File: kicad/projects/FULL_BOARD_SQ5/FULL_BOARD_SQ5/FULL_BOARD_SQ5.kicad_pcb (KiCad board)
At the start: 2 copper layers, 190 parts, among them J2 UART, J4 CONN_2x1, Q1 BC847, SW1 TL3342F450QG, U1 24LC512, U10 HALL_SENSOR_6, U11 HALL_SENSOR_10, U12 HALL_SENSOR_14, U13 HALL_SENSOR3, U14 HALL_SENSOR7, U15 HALL_SENSOR11, U16 HALL_SENSOR15, U17 HALL_SENSOR4, U18 HALL_SENSOR8, U19 HALL_SENSOR12, U2 STM32L431CCTx, U20 HALL_SENSOR16, U21 CD74HC4067M, U22 HALL_SENSOR_1, U23 HALL_SENSOR_5, U24 HALL_SENSOR_9, U25 HALL_SENSOR_13, U26 HALL_SENSOR_2, U27 HALL_SENSOR_6, U28 HALL_SENSOR_10, U29 HALL_SENSOR_14, U3 AP2112K-3.3, U30 HALL_SENSOR3, U31 HALL_SENSOR7, U32 HALL_SENSOR11, U33 HALL_SENSOR15, U34 HALL_SENSOR4, U35 HALL_SENSOR8, U36 HALL_SENSOR12, U37 HALL_SENSOR16, U38 CD74HC4067M, U39 HALL_SENSOR_1, U4 AP2112K-3.3, U40 HALL_SENSOR_5, U41 HALL_SENSOR_9, U42 HALL_SENSOR_13, U43 HALL_SENSOR_2, U44 HALL_SENSOR_6, U45 HALL_SENSOR_10, U46 HALL_SENSOR_14, U47 HALL_SENSOR3, U48 HALL_SENSOR7, U49 HALL_SENSOR11, U5 HALL_SENSOR_1, U50 HALL_SENSOR15, U51 HALL_SENSOR4, U52 HALL_SENSOR8, U53 HALL_SENSOR12, U54 HALL_SENSOR16, U55 CD74HC4067M, U56 HALL_SENSOR_1, U57 HALL_SENSOR_5, U58 HALL_SENSOR_9, U59 HALL_SENSOR_13, U6 HALL_SENSOR_5, U60 HALL_SENSOR_2, U61 HALL_SENSOR_6, U62 HALL_SENSOR_10, U63 HALL_SENSOR_14, U64 HALL_SENSOR3, U65 HALL_SENSOR7, U66 HALL_SENSOR11, U67 HALL_SENSOR15, U68 HALL_SENSOR4, U69 HALL_SENSOR8, U7 HALL_SENSOR_9, U70 HALL_SENSOR12, U71 HALL_SENSOR16, U72 CD74HC4067M, U8 HALL_SENSOR_13, U9 HALL_SENSOR_2

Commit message: saving work
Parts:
- removed U2: STM32L431CCTx, Package_QFP:LQFP-48_7x7mm_P0.5mm
- added D2: PESD5V0L2BT, PCM_Package_TO_SOT_SMD_AKL:SOT-23, F.Cu at (234.8, 163.9)
- added D7: TVS3V3L4U, PCM_Package_SO_AKL:TSOP-6_1.65x3.05mm_P0.95mm, F.Cu at (234.8, 159.1)
- added J1: Conn_ARM_JTAG_SWD_10, BD125-10-A-0305-0580-L-B:GCT_BD125-10-A-0305-0580-L-B, F.Cu at (233.1, 178.0)
- added J3: USB_C_Receptacle_USB2.0_16P, Connector_USB:USB_C_Receptacle_GCT_USB4105-xx-A_16P_TopMnt_Horizontal, F.Cu at (218.5, 162.1)
- added LS1: CMT-1203-SMT, CMT-1203-SMT:CUI_CMT-1203-SMT, F.Cu at (219.5, 148.5)
- added U73: STM32L433CCTx, Package_QFP:LQFP-48_7x7mm_P0.5mm, F.Cu at (218.4, 172.4)
- added Y1: NX3215SA-32.768KHZ-EXS00A-MU00525, PCM_Crystal_AKL:Crystal_SMD_MicroCrystal_CC7V-T1A-2Pin_3.2x1.5mm_HandSoldering, F.Cu at (234.4, 154.2)
- moved U51 102.5 mm to (303.7, 143.5)
- moved U52 102.5 mm to (303.7, 149.3)
- moved U53 102.5 mm to (303.7, 155.1)
- moved U54 102.5 mm to (303.7, 160.8)
- moved U55 102.5 mm to (288.7, 172.0)
- moved R18 102.5 mm to (297.5, 164.9)
- moved U39 102.5 mm to (284.2, 143.5)
- moved U40 102.5 mm to (284.2, 149.3)
- moved U41 102.5 mm to (284.2, 155.1)
- moved U42 102.5 mm to (284.2, 160.8)
- moved U43 102.5 mm to (290.7, 143.5)
- moved U44 102.5 mm to (290.7, 149.3)
- moved U45 102.5 mm to (290.7, 155.1)
- moved U46 102.5 mm to (290.7, 160.8)
- moved C53 102.5 mm to (310.7, 141.7)
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
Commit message: all footprints and started pcb
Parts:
- U10, U11, U12, U13, U14, U15, U16, U17, U18, U19, U20, U22, U23, U24, U25, U26, U27, U28, U29, U30, U31, U32, U33, U34, U35, U36, U37, U39, U40, U41, U42, U43, U44, U45, U46, U47, U48, U49, U5, U50, U51, U52, U53, U54, U56, U57, U58, U59, U6, U60, U61, U62, U63, U64, U65, U66, U67, U68, U69, U7, U70, U71, U8, U9: footprint Package_TO_SOT_THT:TO-92_Inline -> PCM_Package_TO_SOT_SMD_AKL:SOT-23_Handsoldering
- moved R1 419.8 mm to (620.0, 180.0), turned to 90 degrees
- moved Q1 409.9 mm to (619.0, 173.8), turned to 180 degrees
- moved R9 408.1 mm to (609.5, 222.8), turned to 180 degrees
- moved J4 407.6 mm to (619.2, 241.8), turned to 90 degrees
- moved R10 407.1 mm to (609.5, 218.2), turned to 180 degrees
- moved J3 406.1 mm to (619.6, 226.1), turned to 90 degrees
- moved R2 403.9 mm to (604.5, 164.8), turned to 180 degrees
- moved C13 401.3 mm to (598.8, 242.5), turned to -90 degrees
- moved C12 400.6 mm to (598.8, 233.0), turned to 90 degrees
- moved R8 390.8 mm to (587.0, 246.8), turned to 180 degrees
- moved C15 389.3 mm to (588.0, 242.2), turned to 90 degrees
- moved C14 388.4 mm to (588.0, 235.2), turned to -90 degrees
- moved R7 388.2 mm to (587.0, 231.0), turned to 180 degrees
- moved LS1 386.1 mm to (604.8, 173.8), turned to 90 degrees
- moved D4 385.7 mm to (605.5, 240.5)
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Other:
- board outline added: 501 x 401 mm

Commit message: pcb
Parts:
- moved U18 265.4 mm to (466.5, 116.0)
- moved U20 265.3 mm to (466.0, 153.0)
- moved U14 219.4 mm to (414.0, 115.0)
- moved U16 219.1 mm to (413.5, 149.5)
- moved U12 180.8 mm to (368.5, 150.5)
- moved U10 180.5 mm to (368.5, 115.0)
- moved U8 138.0 mm to (319.0, 150.5)
- moved U6 137.1 mm to (318.5, 115.0)
- moved R16 91.9 mm to (274.0, 187.0)
- moved U19 81.4 mm to (280.0, 151.0)
- moved U17 78.3 mm to (279.5, 115.0)
- moved U21 78.2 mm to (496.4, 137.0)
- moved C23 74.9 mm to (261.5, 187.5)
- moved C30 74.9 mm to (266.3, 187.5)
- moved C17 74.9 mm to (261.5, 169.5)
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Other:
- board size 501 x 401 mm -> 501.1 x 405.8 mm

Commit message: all sensors placed and first connections
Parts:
- added J5: I2C, Connector_PinHeader_2.54mm:PinHeader_1x04_P2.54mm_Vertical, F.Cu at (533.5, 282.9)
- added J6: Conn_02x03_Odd_Even, Connector_PinHeader_2.54mm:PinHeader_2x03_P2.54mm_Vertical, F.Cu at (541.5, 282.9)
- added U1: 24LC512, Package_SO:SOIC-8_3.9x4.9mm_P1.27mm, F.Cu at (539.5, 327.6)
- moved U55 433.3 mm to (488.5, 352.0), turned to -90 degrees
- moved U38 433.3 mm to (487.1, 248.3), turned to -90 degrees
- moved U72 426.8 mm to (485.0, 454.0), turned to -90 degrees
- moved R18 420.7 mm to (484.1, 360.9), turned to -90 degrees
- moved R17 420.6 mm to (482.4, 257.1), turned to -90 degrees
- moved C69 416.4 mm to (501.6, 358.4), turned to -90 degrees
- moved C51 416.0 mm to (499.9, 254.6), turned to -90 degrees
- moved R19 413.8 mm to (480.6, 462.5), turned to -90 degrees
- moved C70 413.2 mm to (498.6, 358.4), turned to -90 degrees
- moved C52 412.8 mm to (496.9, 254.6), turned to -90 degrees
- moved C87 408.8 mm to (497.6, 460.4), turned to -90 degrees
- moved U37 408.2 mm to (475.0, 275.0)
- moved U35 406.8 mm to (475.0, 225.0)
- moved U54 406.7 mm to (475.0, 375.0)
- moved C88 405.6 mm to (494.6, 460.4), turned to -90 degrees
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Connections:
- U10 pad 3: hall6 -> /sensor_matrix0/hall6
- U11 pad 3: hall10 -> /sensor_matrix0/hall10
- U12 pad 3: hall14 -> /sensor_matrix0/hall14
- U13 pad 3: hall3 -> /sensor_matrix0/hall3
- U14 pad 3: hall7 -> /sensor_matrix0/hall7
- U15 pad 3: hall11 -> /sensor_matrix0/hall11
- U16 pad 3: hall15 -> /sensor_matrix0/hall15
- U17 pad 3: hall4 -> /sensor_matrix0/hall4
- U18 pad 3: hall8 -> /sensor_matrix0/hall8
- U19 pad 3: hall12 -> /sensor_matrix0/hall12
- U20 pad 3: hall16 -> /sensor_matrix0/hall16
- U21 pad 16: hall16 -> /sensor_matrix0/hall16
- U21 pad 17: hall15 -> /sensor_matrix0/hall15
- U21 pad 18: hall14 -> /sensor_matrix0/hall14
- U21 pad 19: hall13 -> /sensor_matrix0/hall13
- U21 pad 2: hall8 -> /sensor_matrix0/hall8
- U21 pad 20: hall12 -> /sensor_matrix0/hall12
- U21 pad 21: hall11 -> /sensor_matrix0/hall11
- U21 pad 22: hall10 -> /sensor_matrix0/hall10
- U21 pad 23: hall9 -> /sensor_matrix0/hall9
- U21 pad 3: hall7 -> /sensor_matrix0/hall7
- U21 pad 4: hall6 -> /sensor_matrix0/hall6
- U21 pad 5: hall5 -> /sensor_matrix0/hall5
- U21 pad 6: hall4 -> /sensor_matrix0/hall4
- U21 pad 7: hall3 -> /sensor_matrix0/hall3
- U21 pad 8: hall2 -> /sensor_matrix0/hall2
- U21 pad 9: hall1 -> /sensor_matrix0/hall1
- U22 pad 3: hall1 -> /sensor_matrix1/hall1
- U23 pad 3: hall5 -> /sensor_matrix1/hall5
- U24 pad 3: hall9 -> /sensor_matrix1/hall9
- U25 pad 3: hall13 -> /sensor_matrix1/hall13
- U26 pad 3: hall2 -> /sensor_matrix1/hall2
- U27 pad 3: hall6 -> /sensor_matrix1/hall6
- U28 pad 3: hall10 -> /sensor_matrix1/hall10
- U29 pad 3: hall14 -> /sensor_matrix1/hall14
- U30 pad 3: hall3 -> /sensor_matrix1/hall3
- U31 pad 3: hall7 -> /sensor_matrix1/hall7
- U32 pad 3: hall11 -> /sensor_matrix1/hall11
- U33 pad 3: hall15 -> /sensor_matrix1/hall15
- U34 pad 3: hall4 -> /sensor_matrix1/hall4
- U35 pad 3: hall8 -> /sensor_matrix1/hall8
- U36 pad 3: hall12 -> /sensor_matrix1/hall12
- U37 pad 3: hall16 -> /sensor_matrix1/hall16
- U38 pad 16: hall16 -> /sensor_matrix1/hall16
- U38 pad 17: hall15 -> /sensor_matrix1/hall15
- U38 pad 18: hall14 -> /sensor_matrix1/hall14
- U38 pad 19: hall13 -> /sensor_matrix1/hall13
- U38 pad 2: hall8 -> /sensor_matrix1/hall8
- U38 pad 20: hall12 -> /sensor_matrix1/hall12
- U38 pad 21: hall11 -> /sensor_matrix1/hall11
- U38 pad 22: hall10 -> /sensor_matrix1/hall10
- U38 pad 23: hall9 -> /sensor_matrix1/hall9
- U38 pad 3: hall7 -> /sensor_matrix1/hall7
- U38 pad 4: hall6 -> /sensor_matrix1/hall6
- U38 pad 5: hall5 -> /sensor_matrix1/hall5
- U38 pad 6: hall4 -> /sensor_matrix1/hall4
- U38 pad 7: hall3 -> /sensor_matrix1/hall3
- U38 pad 8: hall2 -> /sensor_matrix1/hall2
- U38 pad 9: hall1 -> /sensor_matrix1/hall1
- U39 pad 3: hall1 -> /sensor_matrix2/hall1
- U40 pad 3: hall5 -> /sensor_matrix2/hall5
- U41 pad 3: hall9 -> /sensor_matrix2/hall9
- U42 pad 3: hall13 -> /sensor_matrix2/hall13
- U43 pad 3: hall2 -> /sensor_matrix2/hall2
- U44 pad 3: hall6 -> /sensor_matrix2/hall6
- U45 pad 3: hall10 -> /sensor_matrix2/hall10
- U46 pad 3: hall14 -> /sensor_matrix2/hall14
- U47 pad 3: hall3 -> /sensor_matrix2/hall3
- U48 pad 3: hall7 -> /sensor_matrix2/hall7
- U49 pad 3: hall11 -> /sensor_matrix2/hall11
- U5 pad 3: hall1 -> /sensor_matrix0/hall1
- U50 pad 3: hall15 -> /sensor_matrix2/hall15
- U51 pad 3: hall4 -> /sensor_matrix2/hall4
- U52 pad 3: hall8 -> /sensor_matrix2/hall8
- U53 pad 3: hall12 -> /sensor_matrix2/hall12
- U54 pad 3: hall16 -> /sensor_matrix2/hall16
- U55 pad 16: hall16 -> /sensor_matrix2/hall16
- U55 pad 17: hall15 -> /sensor_matrix2/hall15
- U55 pad 18: hall14 -> /sensor_matrix2/hall14
- U55 pad 19: hall13 -> /sensor_matrix2/hall13
- U55 pad 2: hall8 -> /sensor_matrix2/hall8
- U55 pad 20: hall12 -> /sensor_matrix2/hall12
- U55 pad 21: hall11 -> /sensor_matrix2/hall11
- U55 pad 22: hall10 -> /sensor_matrix2/hall10
- U55 pad 23: hall9 -> /sensor_matrix2/hall9
- U55 pad 3: hall7 -> /sensor_matrix2/hall7
- U55 pad 4: hall6 -> /sensor_matrix2/hall6
- U55 pad 5: hall5 -> /sensor_matrix2/hall5
- U55 pad 6: hall4 -> /sensor_matrix2/hall4
- U55 pad 7: hall3 -> /sensor_matrix2/hall3
- U55 pad 8: hall2 -> /sensor_matrix2/hall2
- U55 pad 9: hall1 -> /sensor_matrix2/hall1
- U56 pad 3: hall1 -> /sensor_matrix3/hall1
- U57 pad 3: hall5 -> /sensor_matrix3/hall5
- U58 pad 3: hall9 -> /sensor_matrix3/hall9
- U59 pad 3: hall13 -> /sensor_matrix3/hall13
- U6 pad 3: hall5 -> /sensor_matrix0/hall5
- U60 pad 3: hall2 -> /sensor_matrix3/hall2
- U61 pad 3: hall6 -> /sensor_matrix3/hall6
- U62 pad 3: hall10 -> /sensor_matrix3/hall10
- U63 pad 3: hall14 -> /sensor_matrix3/hall14
- U64 pad 3: hall3 -> /sensor_matrix3/hall3
- U65 pad 3: hall7 -> /sensor_matrix3/hall7
- U66 pad 3: hall11 -> /sensor_matrix3/hall11
- U67 pad 3: hall15 -> /sensor_matrix3/hall15
- U68 pad 3: hall4 -> /sensor_matrix3/hall4
- U69 pad 3: hall8 -> /sensor_matrix3/hall8
- U7 pad 3: hall9 -> /sensor_matrix0/hall9
- U70 pad 3: hall12 -> /sensor_matrix3/hall12
- U71 pad 3: hall16 -> /sensor_matrix3/hall16
- U72 pad 16: hall16 -> /sensor_matrix3/hall16
- U72 pad 17: hall15 -> /sensor_matrix3/hall15
- U72 pad 18: hall14 -> /sensor_matrix3/hall14
- U72 pad 19: hall13 -> /sensor_matrix3/hall13
- U72 pad 2: hall8 -> /sensor_matrix3/hall8
- U72 pad 20: hall12 -> /sensor_matrix3/hall12
- U72 pad 21: hall11 -> /sensor_matrix3/hall11
- U72 pad 22: hall10 -> /sensor_matrix3/hall10
- U72 pad 23: hall9 -> /sensor_matrix3/hall9
- U72 pad 3: hall7 -> /sensor_matrix3/hall7
- U72 pad 4: hall6 -> /sensor_matrix3/hall6
- U72 pad 5: hall5 -> /sensor_matrix3/hall5
- U72 pad 6: hall4 -> /sensor_matrix3/hall4
- U72 pad 7: hall3 -> /sensor_matrix3/hall3
- U72 pad 8: hall2 -> /sensor_matrix3/hall2
- U72 pad 9: hall1 -> /sensor_matrix3/hall1
- U73 pad 26: unconnected-(U73-PB13-Pad26) -> USER_BUTTON1
- U73 pad 27: unconnected-(U73-PB14-Pad27) -> USER_BUTTON2
- U73 pad 28: unconnected-(U73-PB15-Pad28) -> USER_BUTTON3
- U8 pad 3: hall13 -> /sensor_matrix0/hall13
- U9 pad 3: hall2 -> /sensor_matrix0/hall2
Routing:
- net /sensor_matrix0/hall9: track 0.00 -> 381.3 mm
- net /sensor_matrix0/hall1: track 0.00 -> 363.4 mm
- net /sensor_matrix0/hall10: track 0.00 -> 329.8 mm
- net /sensor_matrix0/hall2: track 0.00 -> 314.5 mm
- net /sensor_matrix0/hall11: track 0.00 -> 278.4 mm
- net /sensor_matrix0/hall3: track 0.00 -> 265.9 mm
- net /sensor_matrix0/hall12: track 0.00 -> 226.1 mm
- net /sensor_matrix0/hall4: track 0.00 -> 216.8 mm
- net /sensor_matrix0/hall13: track 0.00 -> 173.1 mm
- net /sensor_matrix0/hall5: track 0.00 -> 167.7 mm
- net /sensor_matrix0/hall14: track 0.00 -> 121.3 mm
- net /sensor_matrix0/hall6: track 0.00 -> 119.2 mm
- net /sensor_matrix0/hall7: track 0.00 -> 70.5 mm
- net /sensor_matrix0/hall15: track 0.00 -> 69.5 mm
- net /sensor_matrix0/hall16: track 0.00 -> 31.5 mm
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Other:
- board size 501.1 x 405.8 mm -> 450 x 400 mm

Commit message: some configs
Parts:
- removed the U1 at (541.5, 364.6)
- removed the U1 at (539.5, 327.6)
- added U1: 24LC512, Package_SO:SOIC-8_3.9x4.9mm_P1.27mm, F.Cu at (503.7, 123.8)
- moved D9 268.2 mm to (516.0, 119.2), turned to 180 degrees
- moved R15 267.4 mm to (520.3, 119.2), turned to 0 degrees
- moved D8 260.7 mm to (516.0, 123.0), turned to 180 degrees
- moved R12 259.9 mm to (520.5, 123.0), turned to 0 degrees
- moved D6 253.7 mm to (516.0, 126.5), turned to 180 degrees
- moved R11 252.9 mm to (520.5, 126.5), turned to 0 degrees
- moved J2 251.9 mm to (514.5, 103.8), turned to 90 degrees
- moved C3 242.9 mm to (497.0, 149.2)
- moved Y1 241.9 mm to (499.8, 146.5)
- moved C2 241.4 mm to (497.0, 143.7)
- moved D7 240.8 mm to (528.4, 161.7), turned to 180 degrees
- moved C6 240.6 mm to (516.5, 145.0)
- moved C7 240.6 mm to (516.4, 142.5)
- moved C1 240.3 mm to (506.0, 141.9)
- moved C4 240.3 mm to (506.0, 139.1)
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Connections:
- U73 pad 16: LED_USER2 -> unconnected-(U73-PA6-Pad16)
- U73 pad 17: LED_USER1 -> unconnected-(U73-PA7-Pad17)
- U73 pad 18: LED_ALIVE -> unconnected-(U73-PB0-Pad18)
- U73 pad 38: unconnected-(U73-PA15-Pad38) -> LED_ALIVE
- U73 pad 39: unconnected-(U73-PB3-Pad39) -> LED_USER1
- U73 pad 40: unconnected-(U73-PB4-Pad40) -> LED_USER2
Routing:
- net /sensor_matrix0/hall9: track 381.3 -> 0.00 mm
- net /sensor_matrix0/hall1: track 363.4 -> 0.00 mm
- net /sensor_matrix0/hall10: track 329.8 -> 0.00 mm
- net /sensor_matrix0/hall2: track 314.5 -> 0.00 mm
- net /sensor_matrix0/hall11: track 278.4 -> 0.00 mm
- net /sensor_matrix0/hall3: track 265.9 -> 0.00 mm
- net /sensor_matrix0/hall12: track 226.1 -> 0.00 mm
- net /sensor_matrix0/hall4: track 216.8 -> 0.00 mm
- net /sensor_matrix0/hall13: track 173.1 -> 0.00 mm
- net /sensor_matrix0/hall5: track 167.7 -> 0.00 mm
- net /sensor_matrix0/hall14: track 121.3 -> 0.00 mm
- net /sensor_matrix0/hall6: track 119.2 -> 0.00 mm
- net /sensor_matrix0/hall7: track 70.5 -> 0.00 mm
- net /sensor_matrix0/hall15: track 69.5 -> 0.00 mm
- net NRST: track 0.00 -> 50.9 mm, vias 0 -> 2
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
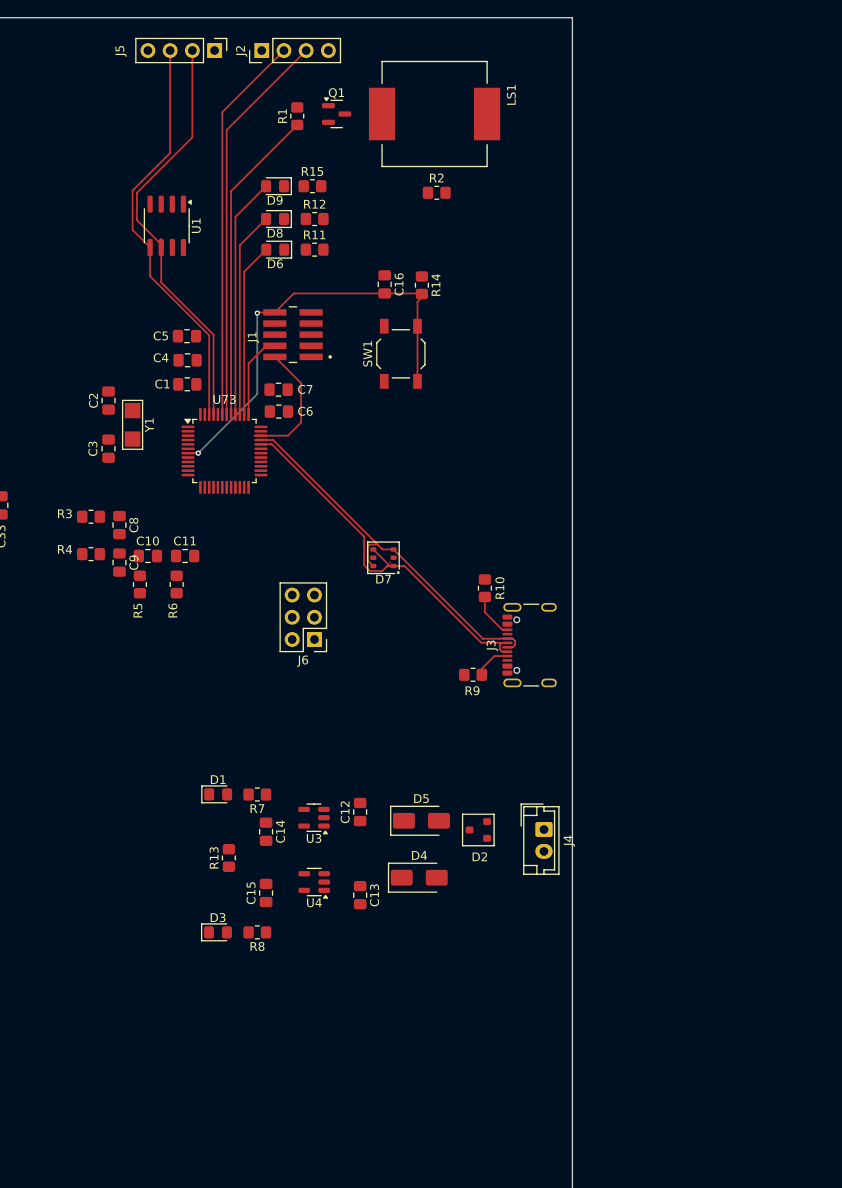
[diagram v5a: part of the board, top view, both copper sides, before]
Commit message: new sensors matrix board
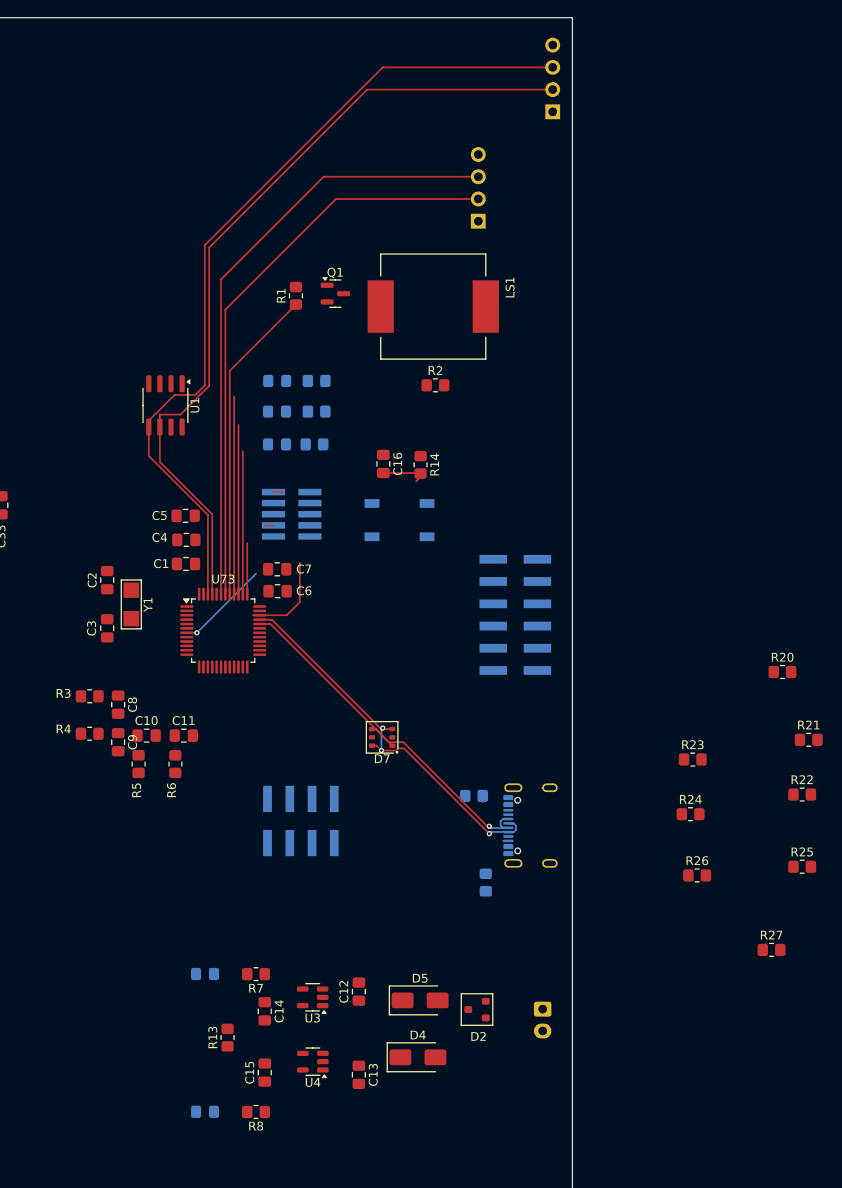
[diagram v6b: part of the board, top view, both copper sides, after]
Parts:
- removed J6: Conn_02x03_Odd_Even, Connector_PinHeader_2.54mm:PinHeader_2x03_P2.54mm_Vertical
- added J7: Conn_02x04_Odd_Even, Connector_PinSocket_2.54mm:PinSocket_2x04_P2.54mm_Vertical_SMD, B.Cu at (519.0, 191.8)
- added J8: Conn_02x06_Odd_Even, Connector_PinHeader_2.54mm:PinHeader_2x06_P2.54mm_Vertical_SMD, B.Cu at (543.5, 168.2)
- added R20: 10k, Resistor_SMD:R_0805_2012Metric_Pad1.20x1.40mm_HandSolder, F.Cu at (574.0, 174.8)
- added R21: 10k, Resistor_SMD:R_0805_2012Metric_Pad1.20x1.40mm_HandSolder, F.Cu at (577.0, 182.5)
- added R22: 10k, Resistor_SMD:R_0805_2012Metric_Pad1.20x1.40mm_HandSolder, F.Cu at (576.2, 188.8)
- added R23: 10k, Resistor_SMD:R_0805_2012Metric_Pad1.20x1.40mm_HandSolder, F.Cu at (563.8, 184.8)
- added R24: 10k, Resistor_SMD:R_0805_2012Metric_Pad1.20x1.40mm_HandSolder, F.Cu at (563.5, 191.0)
- added R25: 10k, Resistor_SMD:R_0805_2012Metric_Pad1.20x1.40mm_HandSolder, F.Cu at (576.2, 197.0)
- added R26: 10k, Resistor_SMD:R_0805_2012Metric_Pad1.20x1.40mm_HandSolder, F.Cu at (564.2, 198.0)
- added R27: 100k, Resistor_SMD:R_0805_2012Metric_Pad1.20x1.40mm_HandSolder, F.Cu at (572.8, 206.5)
- D1, D3, D6, D8, D9, J1, J3, J4, J5, R10, R11, R12, R15, R9, SW1: moved to B.Cu
- J2: footprint Connector_PinHeader_2.54mm:PinHeader_1x04_P2.54mm_Vertical -> Connector_PinHeader_2.54mm:PinHeader_1x04_P2.54mm_Horizontal; moved to B.Cu
- moved J5 39.3 mm to (547.8, 110.8), turned to 0 degrees
- moved R10 33.6 mm to (540.1, 198.8), turned to -90 degrees
- moved J2 31.5 mm to (539.2, 123.2), turned to 0 degrees
- moved D9 29.5 mm to (516.2, 148.8)
- moved R15 29.5 mm to (520.5, 148.8)
- moved D8 22.0 mm to (516.2, 145.0)
- moved R12 22.0 mm to (520.8, 145.0)
- moved LS1 22.0 mm to (534.1, 133.0)
- moved R2 22.0 mm to (534.4, 142.0)
- moved J3 20.6 mm to (546.4, 192.3), turned to -90 degrees
- moved D1 20.6 mm to (508.0, 209.3)
- moved D3 20.6 mm to (508.0, 225.0)
- moved C4 20.5 mm to (505.9, 159.7)
- moved R6 20.5 mm to (504.6, 185.3)
- moved C1 20.5 mm to (505.9, 162.4)
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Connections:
- J2 pad 2: UART_OUT_RX -> UART_OUT_TX
- J2 pad 3: UART_OUT_TX -> UART_OUT_RX
- U73 pad 15: unconnected-(U73-PA5-Pad15) -> NRF24_SCK
- U73 pad 16: unconnected-(U73-PA6-Pad16) -> NRF24_MISO
- U73 pad 17: unconnected-(U73-PA7-Pad17) -> NRF24_MOSI
- U73 pad 18: unconnected-(U73-PB0-Pad18) -> NRF24_CSN
- U73 pad 19: unconnected-(U73-PB1-Pad19) -> FBK_3V3_SENSORS
- U73 pad 20: 3V3_OUT_EN -> NRF24_IRQ
- U73 pad 21: unconnected-(U73-PB10-Pad21) -> EXPANSION0
- U73 pad 22: unconnected-(U73-PB11-Pad22) -> EXPANSION1
- U73 pad 25: unconnected-(U73-PB12-Pad25) -> 3V3_OUT_EN
- U73 pad 26: USER_BUTTON1 -> EXPANSION2
- U73 pad 27: USER_BUTTON2 -> EXPANSION3
- U73 pad 28: USER_BUTTON3 -> EXPANSION4
- U73 pad 29: unconnected-(U73-PA8-Pad29) -> HWREV0
- U73 pad 30: unconnected-(U73-PA9-Pad30) -> HWREV1
- U73 pad 31: unconnected-(U73-PA10-Pad31) -> NRF24_CE
- U73 pad 38: LED_ALIVE -> LED_USER2
- U73 pad 40: LED_USER2 -> LED_ALIVE
- U73 pad 44: unconnected-(U73-PH3-Pad44) -> HWREV3
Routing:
- net I2C_DATA: track 47.0 -> 94.9 mm
- net I2C_CLK: track 48.8 -> 92.5 mm
- net NRST: track 50.9 -> 17.1 mm, vias 2 -> 1
- net UART_OUT_RX: track 44.5 -> 70.2 mm
- net UART_OUT_TX: track 45.3 -> 66.6 mm
- net LED_USER2: track 27.5 -> 16.3 mm
- net Net-(J3-CC2): track 5.15 -> 0.57 mm
- net LED_USER1: track 23.6 -> 19.3 mm
- net SWDIO: track 14.7 -> 10.5 mm
- net Net-(J3-CC1): track 4.22 -> 0.70 mm
- net SWCLK: track 9.67 -> 6.82 mm
- net LED_ALIVE: track 19.9 -> 22.6 mm
- net USB_P: track 43.8 -> 46.3 mm, vias 0 -> 3
- net USB_N: track 45.6 -> 44.1 mm, vias 0 -> 1
